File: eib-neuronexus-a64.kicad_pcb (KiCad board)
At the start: 2 copper layers, 53 x 59 mm, 4 parts, among them J1 xOLC-110-01-S-Q_1, J2 xOLC-110-01-S-Q_1, J3 Conn_02x35_Odd_Even, J4 Conn_01x02_Male

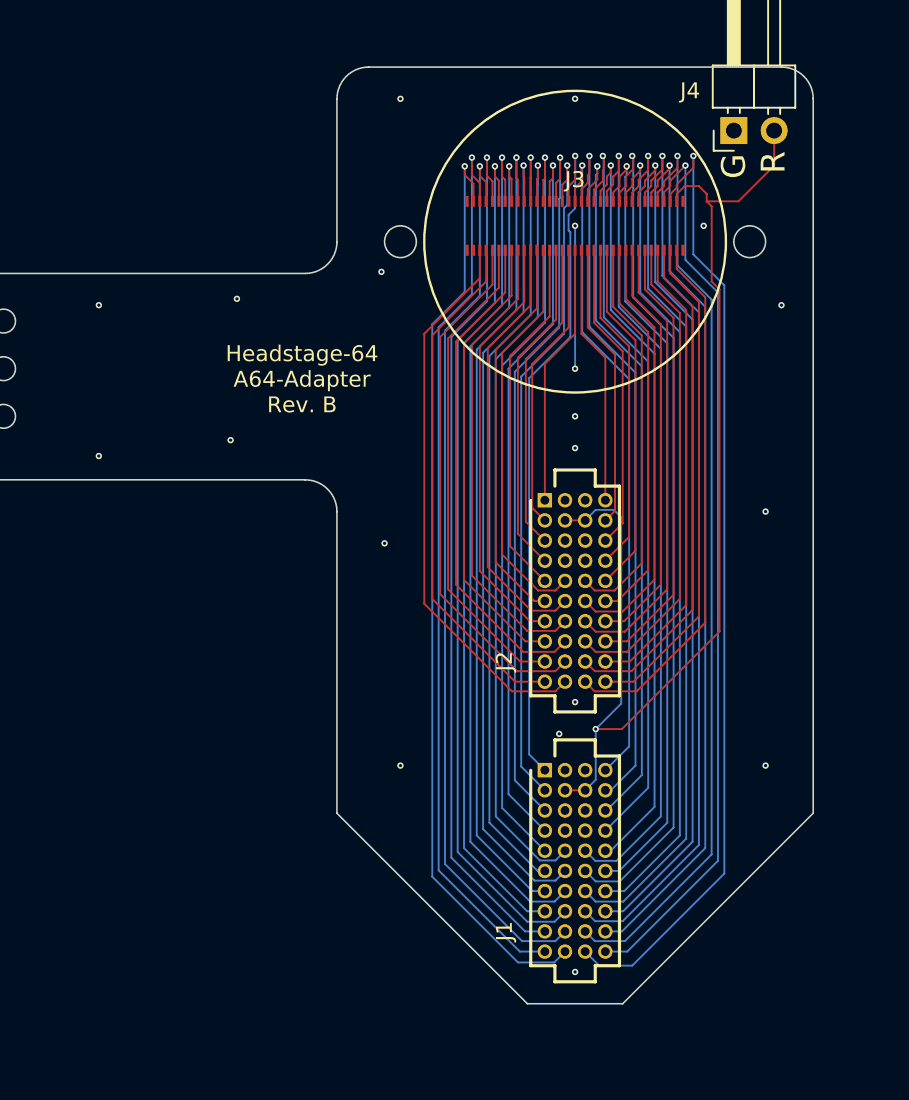
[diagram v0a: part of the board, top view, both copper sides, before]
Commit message: Updated with alternative SMD package for big 5x8 connector
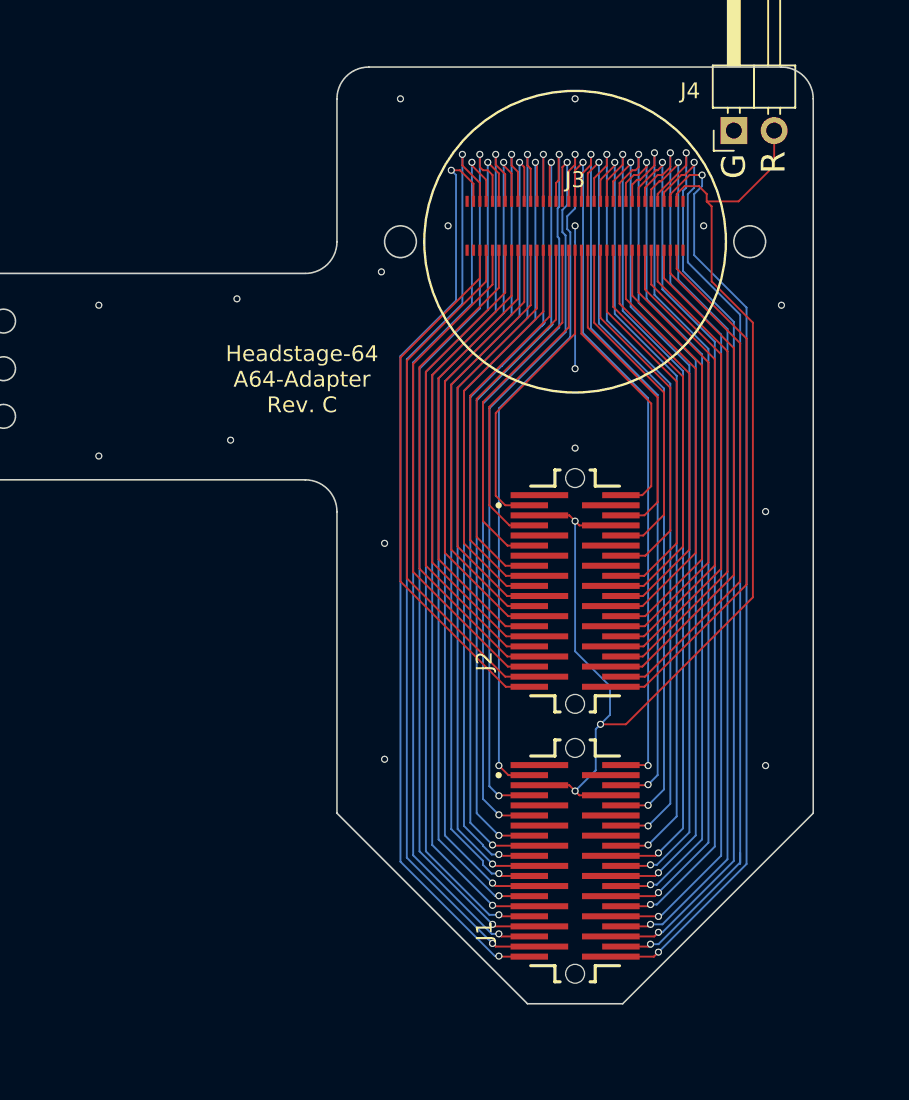
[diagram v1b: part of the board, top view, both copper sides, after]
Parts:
- J1, J2: footprint jonnew:SAMTEC_FOLC-110-01-S-Q -> FOLC:SAMTEC_FOLC-110-02-S-Q-LC
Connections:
- J1 pad A10: /Elec62 -> /Elec63
- J1 pad A5: /Elec52 -> /Elec53
- J1 pad A6: /Elec54 -> /Elec55
- J1 pad A7: /Elec56 -> /Elec57
- J1 pad A8: /Elec58 -> /Elec59
- J1 pad A9: /Elec60 -> /Elec61
- J1 pad B10: /Elec63 -> /Elec62
- J1 pad B5: /Elec53 -> /Elec52
- J1 pad B6: /Elec55 -> /Elec54
- J1 pad B7: /Elec57 -> /Elec56
- J1 pad B8: /Elec59 -> /Elec58
- J1 pad B9: /Elec61 -> /Elec60
- J2 pad A10: /Elec46 -> /Elec47
- J2 pad A5: /Elec36 -> /Elec37
- J2 pad A6: /Elec38 -> /Elec39
- J2 pad A7: /Elec40 -> /Elec41
- J2 pad A8: /Elec42 -> /Elec43
- J2 pad A9: /Elec44 -> /Elec45
- J2 pad B10: /Elec47 -> /Elec46
- J2 pad B5: /Elec37 -> /Elec36
- J2 pad B6: /Elec39 -> /Elec38
- J2 pad B7: /Elec41 -> /Elec40
- J2 pad B8: /Elec43 -> /Elec42
- J2 pad B9: /Elec45 -> /Elec44
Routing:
- net /Ref: track 71.8 -> 78.0 mm, vias 1 -> 3
- net /Elec52: track 48.7 -> 52.2 mm, vias 1 -> 2
- net /Elec51: track 46.4 -> 49.8 mm, vias 1 -> 2
- net /Elec32: track 16.5 -> 19.9 mm
- net /Elec49: track 43.6 -> 46.9 mm, vias 1 -> 2
- net /Elec50: track 46.0 -> 49.1 mm, vias 1 -> 2
- net /Elec54: track 50.5 -> 53.5 mm, vias 1 -> 2
- net /Elec34: track 19.7 -> 22.7 mm
- net /Elec35: track 21.3 -> 24.2 mm
- net /Elec33: track 18.3 -> 21.2 mm
- net /Elec36: track 22.8 -> 25.6 mm
- net /Elec56: track 52.3 -> 55.0 mm, vias 1 -> 2
- net /Elec60: track 55.8 -> 58.4 mm, vias 1 -> 2
- net /Elec58: track 54.1 -> 56.7 mm, vias 1 -> 2
- net /Elec48: track 43.4 -> 45.9 mm, vias 1 -> 2
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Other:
- board text added: "Headstage-64 A64-Adapter Rev. C"
- board text removed: "Headstage-64 A64-Adapter Rev. B"
